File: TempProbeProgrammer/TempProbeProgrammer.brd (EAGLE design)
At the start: 18.4 x 13.3 mm, 15 parts, among them U2 ATTINY841

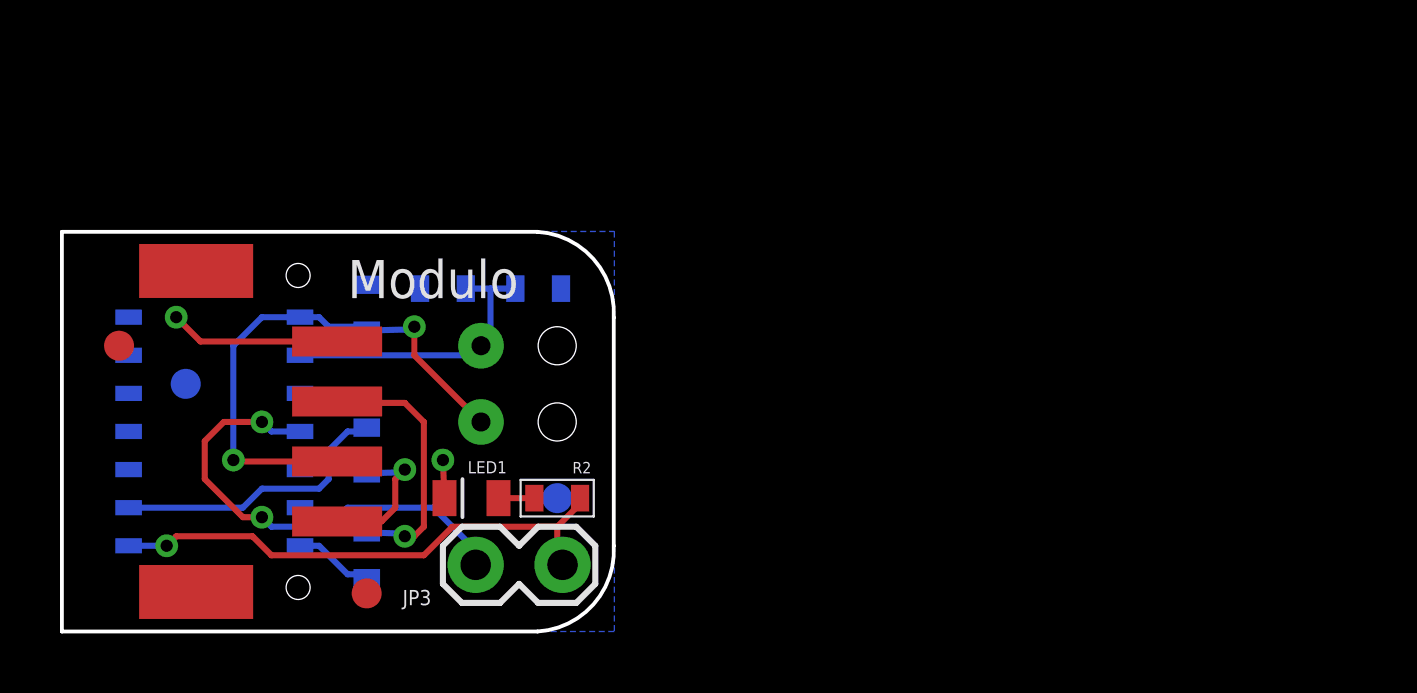
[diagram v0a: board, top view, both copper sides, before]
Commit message: Revised temperature probe layout and created new temp probe programmer board
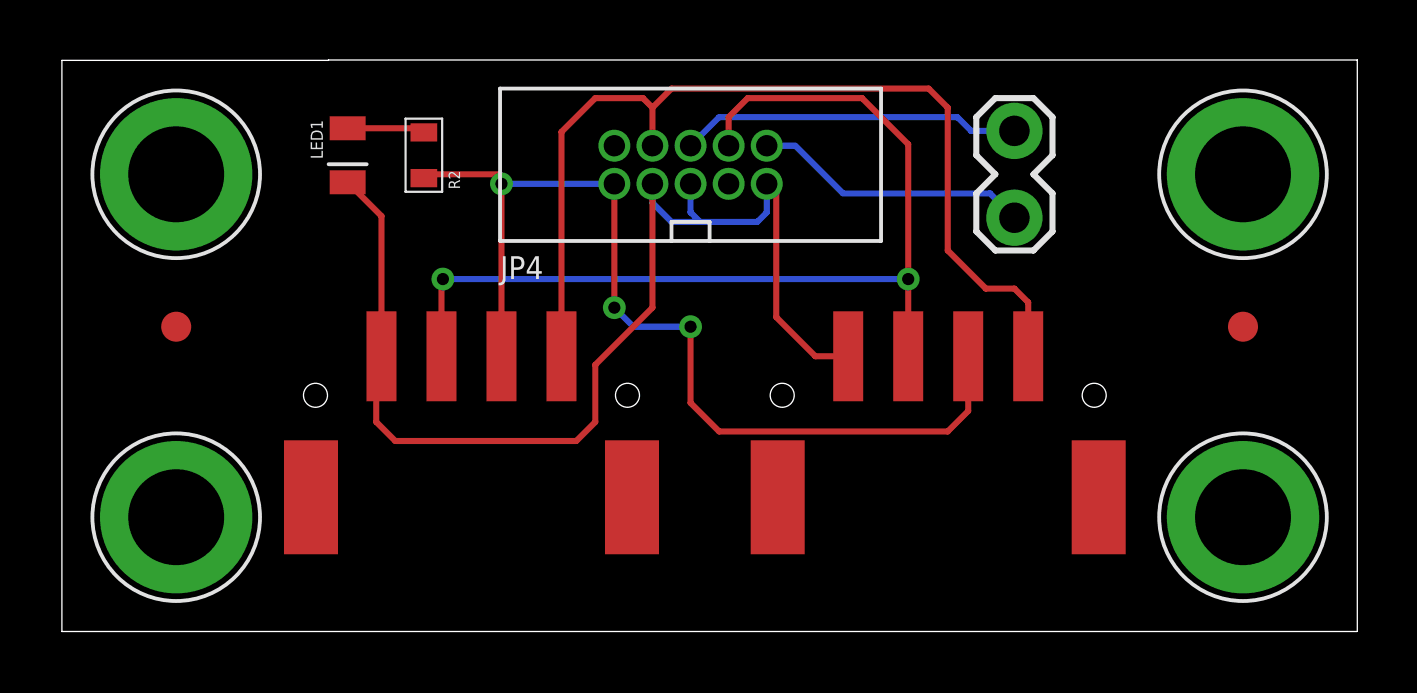
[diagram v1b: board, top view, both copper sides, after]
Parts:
- removed C1, C2: .1uF, Modulo:0603
- removed F2, F4: FIDUCIAL, Modulo:FIDUCIAL_1MM
- removed PROBE1: TEMP-PROBE, Modulo:TEMP_PROBE
- removed R1: 10KΩ, Modulo:0603
- removed R8, R9: 150Ω, Modulo:0603
- removed U2: ATTINY841, Modulo:SOIC-14
- added H1, H2, H3, H4: HOLE#4, Modulo:HOLE-#4
- added JP2: HEADER-1X4-JST-PA-SIDE-SMD, Modulo:JST-PA-SIDE-SMD
- added JP4: ICSP, Modulo:2X5-.05
- moved F1 37.5 mm to (39.4, 10.2)
- moved JP3 20.9 mm to (31.8, 16.5), turned to 270 degrees
- moved JP1 15.2 mm to (13.7, 0.00), turned to 0 degrees
- moved R2 12.3 mm to (12.1, 15.9), turned to 270 degrees
- moved LED1 12.2 mm to (9.53, 15.9), turned to 180 degrees
- moved F3 10.9 mm to (3.81, 10.2)
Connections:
- removed net MISO/LED: JP3.1, R2.2, U2.8
- removed net SCL: JP1.4, R8.1
- removed net SDA: JP1.2, R9.1
- removed net TEMP: C2.2, PROBE1.P$1, R1.2, U2.2
- new net MISO: JP3.1, JP4.6
- new net SWDIO: JP4.2
- net GND: now also JP2.1, JP4.3, JP4.5, JP4.9; no longer C1.2, C2.1, R1.1, U2.14
- net RESET: now also JP4.10; no longer U2.4
- net SCL/SCK: now also JP1.4, JP2.4, JP4.4; no longer R8.2, U2.9
- net SDA/MOSI: now also JP1.2, JP2.2, JP4.8; no longer R9.2, U2.7
- net VCC: now also JP2.3, JP4.1, R2.2; no longer C1.1, PROBE1.P$2, U2.1
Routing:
- net GND: track 6.97 -> 39.8 mm, vias 2 -> 0
- net SDA/MOSI: track 2.68 -> 33.0 mm, vias 0 -> 2
- net SCL/SCK: track 9.61 -> 32.7 mm
- net MISO/LED: track 17.7 -> 0.00 mm, vias 1 -> 0
- net VCC: track 18.0 -> 33.7 mm, vias 2 -> 3
- net MISO: track 0.00 -> 11.4 mm
- net TEMP: track 9.85 -> 0.00 mm
- net SDA: track 8.74 -> 0.00 mm, vias 1 -> 0
- net RESET: track 15.9 -> 9.25 mm, vias 2 -> 0
- net SCL: track 4.84 -> 0.00 mm, vias 1 -> 0
- net N$2: track 1.20 -> 2.60 mm
- removed copper zone on layer 16, net GND
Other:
- board size 18.4 x 13.3 mm -> 43.2 x 19.1 mm
- board text removed: "Modulo"
- board text removed: "TempProbe v4"
